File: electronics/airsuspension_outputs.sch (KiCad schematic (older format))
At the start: 51 parts, among them Q1 BSS138, Q2 BC847, U1 ITS5215L, U2 BTS6133D, U3 ITS5215L, U4 ITS5215L, U5 ITS5215L

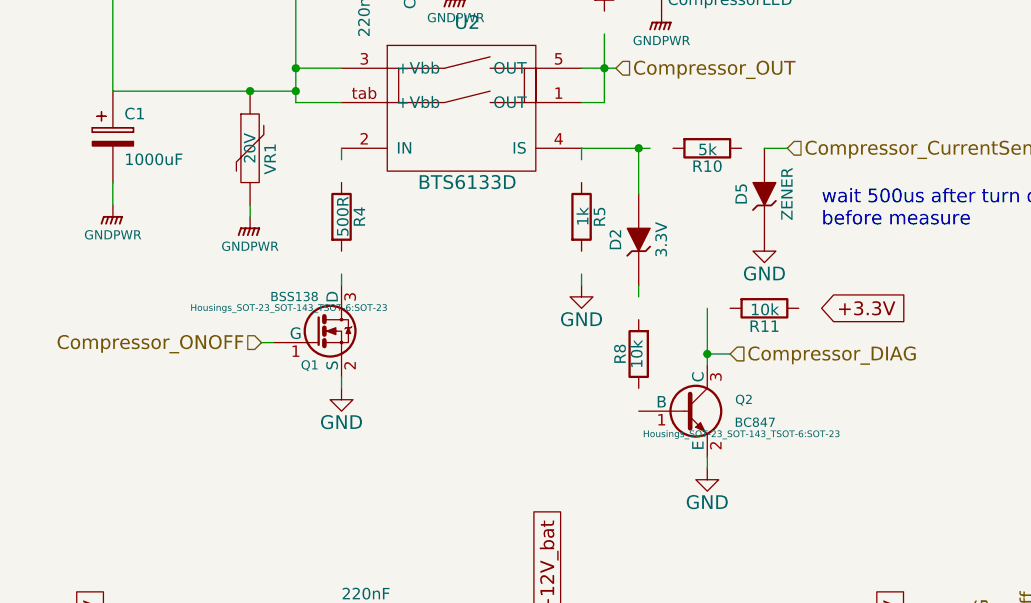
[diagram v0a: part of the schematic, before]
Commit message: Some more fottprints added to PCB
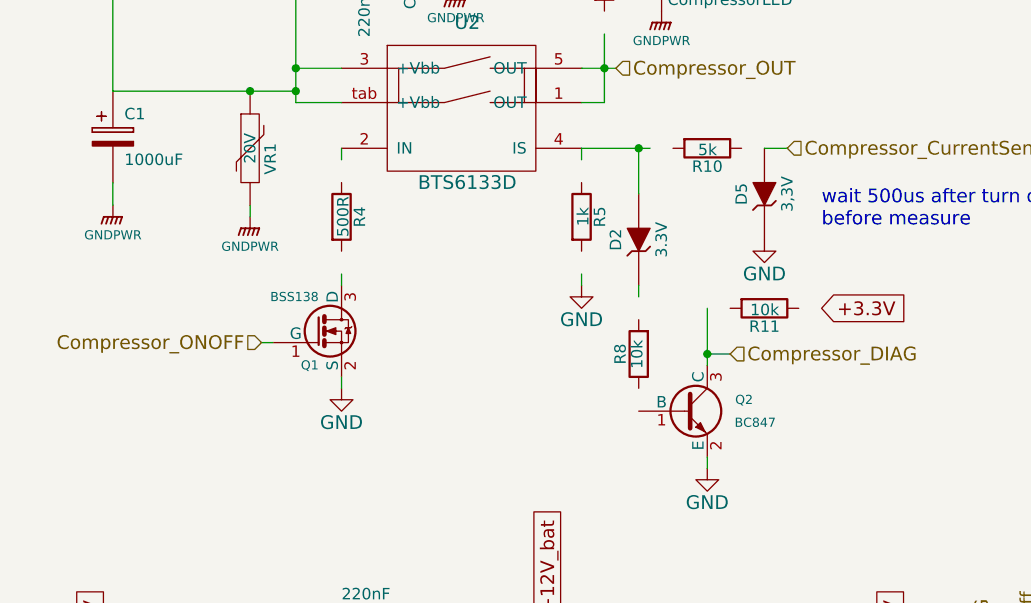
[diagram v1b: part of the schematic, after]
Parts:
- C2, C3, C4, C5, C6: footprint (none) -> Capacitors_SMD:C_0805; farnell (none) -> 1288261; name (none) -> C0805C224K5RACTU
- D2: footprint (none) -> Diodes_SMD:SOD-323
- D5: value ZENER -> 3,3V; footprint (none) -> Diodes_SMD:SOD-323
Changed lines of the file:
@@
 F 0 "C3" H 2750 1200 50  0000 L CNN
 F 1 "220nF" H 2750 1000 50  0000 L CNN
-F 2 "" H 2738 950 30  0001 C CNN
+F 2 "Capacitors_SMD:C_0805" H 2738 950 30  0001 C CNN
 F 3 "" H 2700 1100 60  0000 C CNN
+F 4 "1288261" H 2700 1100 60  0001 C CNN "farnell"
+F 5 "C0805C224K5RACTU" H 2700 1100 60  0001 C CNN "name"
 	1    2700 1100
 	0    1    1    0
@@
 F 0 "C2" H 2650 4050 50  0000 L CNN
 F 1 "220nF" V 2450 3850 50  0000 L CNN
-F 2 "" H 2638 3800 30  0001 C CNN
+F 2 "Capacitors_SMD:C_0805" H 2638 3800 30  0001 C CNN
 F 3 "" H 2600 3950 60  0000 C CNN
+F 4 "1288261" H 2600 3950 60  0001 C CNN "farnell"
+F 5 "C0805C224K5RACTU" H 2600 3950 60  0001 C CNN "name"
 	1    2600 3950
 	0    1    1    0
@@
 F 0 "D2" H 3800 2350 50  0000 C CNN
 F 1 "3.3V" H 3800 2150 50  0000 C CNN
-F 2 "" H 3800 2250 60  0001 C CNN
+F 2 "Diodes_SMD:SOD-323" H 3800 2250 60  0001 C CNN
 F 3 "" H 3800 2250 60  0000 C CNN
 F 4 "PDZ3.3B,115" H 3800 2250 60  0001 C CNN "name"
@@
 P 4350 2050
 F 0 "D5" H 4350 2150 50  0000 C CNN
-F 1 "ZENER" H 4350 1950 50  0000 C CNN
-F 2 "" H 4350 2050 60  0001 C CNN
+F 1 "3,3V" H 4350 1950 50  0000 C CNN
+F 2 "Diodes_SMD:SOD-323" H 4350 2050 60  0001 C CNN
 F 3 "" H 4350 2050 60  0000 C CNN
 F 4 "PDZ3.3B,115" H 4350 2050 60  0001 C CNN "name"
@@
 F 0 "C5" H 8300 1100 50  0000 L CNN
 F 1 "220nF" V 8100 900 50  0000 L CNN
-F 2 "" H 8288 850 30  0001 C CNN
+F 2 "Capacitors_SMD:C_0805" H 8288 850 30  0001 C CNN
 F 3 "" H 8250 1000 60  0000 C CNN
+F 4 "1288261" H 8250 1000 60  0001 C CNN "farnell"
+F 5 "C0805C224K5RACTU" H 8250 1000 60  0001 C CNN "name"
 	1    8250 1000
 	0    1    1    0
@@
 F 0 "C6" H 9350 4050 50  0000 L CNN
 F 1 "220nF" V 9150 3850 50  0000 L CNN
-F 2 "" H 9338 3800 30  0001 C CNN
+F 2 "Capacitors_SMD:C_0805" H 9338 3800 30  0001 C CNN
 F 3 "" H 9300 3950 60  0000 C CNN
+F 4 "1288261" H 9300 3950 60  0001 C CNN "farnell"
+F 5 "C0805C224K5RACTU" H 9300 3950 60  0001 C CNN "name"
 	1    9300 3950
 	0    1    1    0
@@
 F 0 "C4" H 6150 4050 50  0000 L CNN
 F 1 "220nF" V 5950 3850 50  0000 L CNN
-F 2 "" H 6138 3800 30  0001 C CNN
+F 2 "Capacitors_SMD:C_0805" H 6138 3800 30  0001 C CNN
 F 3 "" H 6100 3950 60  0000 C CNN
+F 4 "1288261" H 6100 3950 60  0001 C CNN "farnell"
+F 5 "C0805C224K5RACTU" H 6100 3950 60  0001 C CNN "name"
 	1    6100 3950
 	0    1    1    0
@@
 F 0 "Q2" H 4300 3050 40  0000 R CNN
 F 1 "BC847" H 4400 2950 40  0000 R CNN
-F 2 "Housings_SOT-23_SOT-143_TSOT-6:SOT-23" H 4250 2900 29  0000 C CNN
+F 2 "Housings_SOT-23_SOT-143_TSOT-6:SOT-23" H 4250 2900 29  0001 C CNN
 F 3 "" H 4000 3000 60  0000 C CNN
 F 4 "1773609" H 4000 3000 60  0001 C CNN "farnell"
@@
 F 0 "Q1" H 2400 2501 40  0000 R CNN
 F 1 "BSS138" H 2400 2800 40  0000 R CNN
-F 2 "Housings_SOT-23_SOT-143_TSOT-6:SOT-23" H 2270 2752 29  0000 C CNN
+F 2 "Housings_SOT-23_SOT-143_TSOT-6:SOT-23" H 2270 2752 29  0001 C CNN
 F 3 "" H 2400 2650 60  0000 C CNN
 F 4 "2053833" H 2400 2650 60  0001 C CNN "farnell"

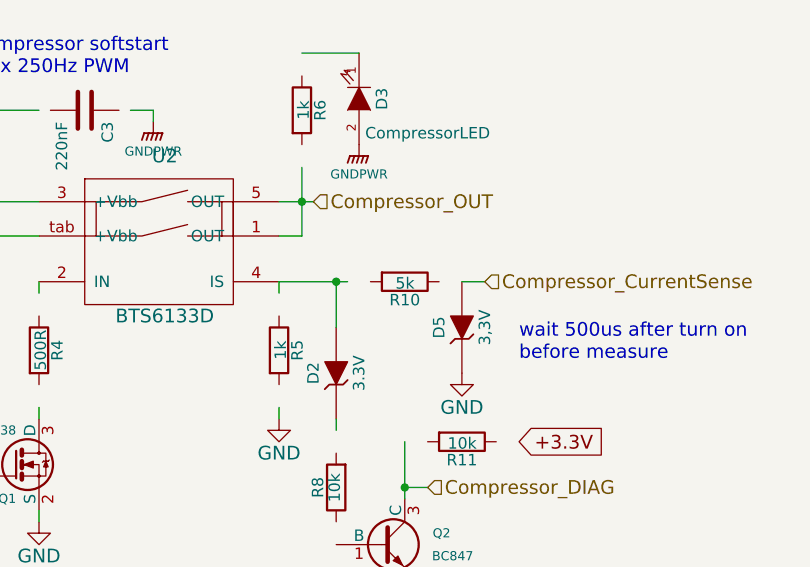
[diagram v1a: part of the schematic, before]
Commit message: some fottprints and BOM changes
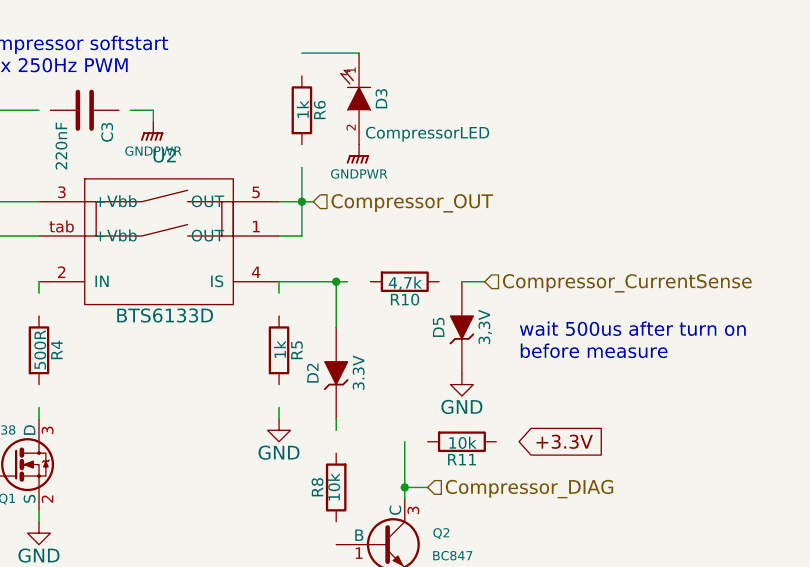
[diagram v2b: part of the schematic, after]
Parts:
- R1, R12, R13, R15, R16, R17, R18, R2, R20, R21, R23, R24, R25, R26, R5, R7, R9: footprint (none) -> Resistors_SMD:R_0805; farnell (none) -> 1577659; name (none) -> ERA6AEB102V
- R10: value 5k -> 4,7k; footprint (none) -> Resistors_SMD:R_0805; farnell (none) -> 2333572; name (none) -> CR0805-FX-4701ELF
- R11, R8: footprint (none) -> Resistors_SMD:R_0805; farnell (none) -> 612522; name (none) -> CR0805-FX-1002ELF
- R14, R19, R22, R3: footprint (none) -> Resistors_SMD:R_0805; farnell (none) -> 2303460; name (none) -> ERJ6ENF1500V
- R4: footprint (none) -> Resistors_SMD:R_0805; farnell (none) -> 2303491; name (none) -> ERJ6ENF3000V
- R6: footprint (none) -> Resistors_SMD:R_0805
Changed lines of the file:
@@
 F 0 "R4" V 2580 2150 50  0000 C CNN
 F 1 "500R" V 2507 2151 50  0000 C CNN
-F 2 "" V 2430 2150 30  0001 C CNN
+F 2 "Resistors_SMD:R_0805" V 2430 2150 30  0001 C CNN
 F 3 "" H 2500 2150 30  0000 C CNN
+F 4 "2303491" V 2500 2150 60  0001 C CNN "farnell"
+F 5 "ERJ6ENF3000V" V 2500 2150 60  0001 C CNN "name"
 	1    2500 2150
 	1    0    0    -1
@@
 F 0 "R5" V 3630 2150 50  0000 C CNN
 F 1 "1k" V 3557 2151 50  0000 C CNN
-F 2 "" V 3480 2150 30  0001 C CNN
+F 2 "Resistors_SMD:R_0805" V 3480 2150 30  0001 C CNN
 F 3 "" H 3550 2150 30  0000 C CNN
+F 4 "1577659" V 3550 2150 60  0001 C CNN "farnell"
+F 5 "ERA6AEB102V" V 3550 2150 60  0001 C CNN "name"
 	1    3550 2150
 	1    0    0    -1
@@
 F 0 "R8" V 3880 2750 50  0000 C CNN
 F 1 "10k" V 3807 2751 50  0000 C CNN
-F 2 "" V 3730 2750 30  0001 C CNN
+F 2 "Resistors_SMD:R_0805" V 3730 2750 30  0001 C CNN
 F 3 "" H 3800 2750 30  0000 C CNN
+F 4 "CR0805-FX-1002ELF" V 3800 2750 60  0001 C CNN "name"
+F 5 "612522" V 3800 2750 60  0001 C CNN "farnell"
 	1    3800 2750
 	-1   0    0    1
@@
 P 4100 1850
 F 0 "R10" V 4180 1850 50  0000 C CNN
-F 1 "5k" V 4107 1851 50  0000 C CNN
-F 2 "" V 4030 1850 30  0001 C CNN
+F 1 "4,7k" V 4107 1851 50  0000 C CNN
+F 2 "Resistors_SMD:R_0805" V 4030 1850 30  0001 C CNN
 F 3 "" H 4100 1850 30  0000 C CNN
+F 4 "2333572" V 4100 1850 60  0001 C CNN "farnell"
+F 5 "CR0805-FX-4701ELF" V 4100 1850 60  0001 C CNN "name"
 	1    4100 1850
 	0    1    1    0
@@
 F 0 "R11" V 4430 2550 50  0000 C CNN
 F 1 "10k" V 4357 2551 50  0000 C CNN
-F 2 "" V 4280 2550 30  0001 C CNN
+F 2 "Resistors_SMD:R_0805" V 4280 2550 30  0001 C CNN
 F 3 "" H 4350 2550 30  0000 C CNN
+F 4 "612522" V 4350 2550 60  0001 C CNN "farnell"
+F 5 "CR0805-FX-1002ELF" V 4350 2550 60  0001 C CNN "name"
 	1    4350 2550
 	0    1    1    0
@@
 F 0 "R6" V 3730 1100 50  0000 C CNN
 F 1 "1k" V 3657 1101 50  0000 C CNN
-F 2 "" V 3580 1100 30  0001 C CNN
+F 2 "Resistors_SMD:R_0805" V 3580 1100 30  0001 C CNN
 F 3 "" H 3650 1100 30  0000 C CNN
 	1    3650 1100
@@
 F 0 "R2" V 1680 4500 50  0000 C CNN
 F 1 "1k" V 1607 4501 50  0000 C CNN
-F 2 "" V 1530 4500 30  0001 C CNN
+F 2 "Resistors_SMD:R_0805" V 1530 4500 30  0001 C CNN
 F 3 "" H 1600 4500 30  0000 C CNN
+F 4 "ERA6AEB102V" V 1600 4500 60  0001 C CNN "name"
+F 5 "1577659" V 1600 4500 60  0001 C CNN "farnell"
 	1    1600 4500
 	-1   0    0    1
@@
 F 0 "R1" V 1480 4500 50  0000 C CNN
 F 1 "1k" V 1407 4501 48  0000 C CNN
-F 2 "" V 1330 4500 30  0001 C CNN
+F 2 "Resistors_SMD:R_0805" V 1330 4500 30  0001 C CNN
 F 3 "" H 1400 4500 30  0000 C CNN
+F 4 "ERA6AEB102V" V 1400 4500 60  0001 C CNN "name"
+F 5 "1577659" V 1400 4500 60  0001 C CNN "farnell"
 	1    1400 4500
 	-1   0    0    1
@@
 F 0 "R7" V 3730 5400 50  0000 C CNN
 F 1 "1k" V 3657 5401 50  0000 C CNN
-F 2 "" V 3580 5400 30  0001 C CNN
+F 2 "Resistors_SMD:R_0805" V 3580 5400 30  0001 C CNN
 F 3 "" H 3650 5400 30  0000 C CNN
+F 4 "ERA6AEB102V" V 3650 5400 60  0001 C CNN "name"
+F 5 "1577659" V 3650 5400 60  0001 C CNN "farnell"
 	1    3650 5400
 	-1   0    0    1
@@
 F 0 "R9" V 3980 5400 50  0000 C CNN
 F 1 "1k" V 3907 5401 50  0000 C CNN
-F 2 "" V 3830 5400 30  0001 C CNN
+F 2 "Resistors_SMD:R_0805" V 3830 5400 30  0001 C CNN
 F 3 "" H 3900 5400 30  0000 C CNN
+F 4 "ERA6AEB102V" V 3900 5400 60  0001 C CNN "name"
+F 5 "1577659" V 3900 5400 60  0001 C CNN "farnell"
 	1    3900 5400
 	1    0    0    -1
@@
 F 0 "R3" V 2230 4200 50  0000 C CNN
 F 1 "150R" V 2157 4201 50  0000 C CNN
-F 2 "" V 2080 4200 30  0001 C CNN
+F 2 "Resistors_SMD:R_0805" V 2080 4200 30  0001 C CNN
 F 3 "" H 2150 4200 30  0000 C CNN
+F 4 "ERJ6ENF1500V" V 2150 4200 60  0001 C CNN "name"
+F 5 "2303460" V 2150 4200 60  0001 C CNN "farnell"
 	1    2150 4200
 	1    0    0    -1
@@
 F 0 "R17" V 7330 1550 50  0000 C CNN
 F 1 "1k" V 7257 1551 50  0000 C CNN
-F 2 "" V 7180 1550 30  0001 C CNN
+F 2 "Resistors_SMD:R_0805" V 7180 1550 30  0001 C CNN
 F 3 "" H 7250 1550 30  0000 C CNN
+F 4 "ERA6AEB102V" V 7250 1550 60  0001 C CNN "name"
+F 5 "1577659" V 7250 1550 60  0001 C CNN "farnell"
 	1    7250 1550
 	-1   0    0    1
@@
 F 0 "R15" V 7130 1550 50  0000 C CNN
 F 1 "1k" V 7057 1551 48  0000 C CNN
-F 2 "" V 6980 1550 30  0001 C CNN
+F 2 "Resistors_SMD:R_0805" V 6980 1550 30  0001 C CNN
 F 3 "" H 7050 1550 30  0000 C CNN
+F 4 "ERA6AEB102V" V 7050 1550 60  0001 C CNN "name"
+F 5 "1577659" V 7050 1550 60  0001 C CNN "farnell"
 	1    7050 1550
 	-1   0    0    1
@@
 F 0 "R23" V 9380 2450 50  0000 C CNN
 F 1 "1k" V 9307 2451 50  0000 C CNN
-F 2 "" V 9230 2450 30  0001 C CNN
+F 2 "Resistors_SMD:R_0805" V 9230 2450 30  0001 C CNN
 F 3 "" H 9300 2450 30  0000 C CNN
+F 4 "ERA6AEB102V" V 9300 2450 60  0001 C CNN "name"
+F 5 "1577659" V 9300 2450 60  0001 C CNN "farnell"
 	1    9300 2450
 	-1   0    0    1
@@
 F 0 "R24" V 9630 2450 50  0000 C CNN
 F 1 "1k" V 9557 2451 50  0000 C CNN
-F 2 "" V 9480 2450 30  0001 C CNN
+F 2 "Resistors_SMD:R_0805" V 9480 2450 30  0001 C CNN
 F 3 "" H 9550 2450 30  0000 C CNN
+F 4 "ERA6AEB102V" V 9550 2450 60  0001 C CNN "name"
+F 5 "1577659" V 9550 2450 60  0001 C CNN "farnell"
 	1    9550 2450
 	1    0    0    -1
@@
 F 0 "R19" V 7880 1250 50  0000 C CNN
 F 1 "150R" V 7807 1251 50  0000 C CNN
-F 2 "" V 7730 1250 30  0001 C CNN
+F 2 "Resistors_SMD:R_0805" V 7730 1250 30  0001 C CNN
 F 3 "" H 7800 1250 30  0000 C CNN
+F 4 "2303460" V 7800 1250 60  0001 C CNN "farnell"
+F 5 "ERJ6ENF1500V" V 7800 1250 60  0001 C CNN "name"
 	1    7800 1250
 	1    0    0    -1
@@
 F 0 "R21" V 8380 4500 50  0000 C CNN
 F 1 "1k" V 8307 4501 50  0000 C CNN
-F 2 "" V 8230 4500 30  0001 C CNN
+F 2 "Resistors_SMD:R_0805" V 8230 4500 30  0001 C CNN
 F 3 "" H 8300 4500 30  0000 C CNN
+F 4 "ERA6AEB102V" V 8300 4500 60  0001 C CNN "name"
+F 5 "1577659" V 8300 4500 60  0001 C CNN "farnell"
 	1    8300 4500
 	-1   0    0    1
@@
 F 0 "R20" V 8180 4500 50  0000 C CNN
 F 1 "1k" V 8107 4501 48  0000 C CNN
-F 2 "" V 8030 4500 30  0001 C CNN
+F 2 "Resistors_SMD:R_0805" V 8030 4500 30  0001 C CNN
 F 3 "" H 8100 4500 30  0000 C CNN
+F 4 "ERA6AEB102V" V 8100 4500 60  0001 C CNN "name"
+F 5 "1577659" V 8100 4500 60  0001 C CNN "farnell"
 	1    8100 4500
 	-1   0    0    1
@@
 F 0 "R25" V 10430 5400 50  0000 C CNN
 F 1 "1k" V 10357 5401 50  0000 C CNN
-F 2 "" V 10280 5400 30  0001 C CNN
+F 2 "Resistors_SMD:R_0805" V 10280 5400 30  0001 C CNN
 F 3 "" H 10350 5400 30  0000 C CNN
+F 4 "ERA6AEB102V" V 10350 5400 60  0001 C CNN "name"
+F 5 "1577659" V 10350 5400 60  0001 C CNN "farnell"
 	1    10350 5400
 	-1   0    0    1
@@
 F 0 "R26" V 10680 5400 50  0000 C CNN
 F 1 "1k" V 10607 5401 50  0000 C CNN
-F 2 "" V 10530 5400 30  0001 C CNN
+F 2 "Resistors_SMD:R_0805" V 10530 5400 30  0001 C CNN
 F 3 "" H 10600 5400 30  0000 C CNN
+F 4 "ERA6AEB102V" V 10600 5400 60  0001 C CNN "name"
+F 5 "1577659" V 10600 5400 60  0001 C CNN "farnell"
 	1    10600 5400
 	1    0    0    -1
@@
 F 0 "R22" V 8930 4200 50  0000 C CNN
 F 1 "150R" V 8857 4201 50  0000 C CNN
-F 2 "" V 8780 4200 30  0001 C CNN
+F 2 "Resistors_SMD:R_0805" V 8780 4200 30  0001 C CNN
 F 3 "" H 8850 4200 30  0000 C CNN
+F 4 "ERJ6ENF1500V" V 8850 4200 60  0001 C CNN "name"
+F 5 "2303460" V 8850 4200 60  0001 C CNN "farnell"
 	1    8850 4200
 	1    0    0    -1
@@
 F 0 "R13" V 5180 4500 50  0000 C CNN
 F 1 "1k" V 5107 4501 50  0000 C CNN
-F 2 "" V 5030 4500 30  0001 C CNN
+F 2 "Resistors_SMD:R_0805" V 5030 4500 30  0001 C CNN
 F 3 "" H 5100 4500 30  0000 C CNN
+F 4 "ERA6AEB102V" V 5100 4500 60  0001 C CNN "name"
+F 5 "1577659" V 5100 4500 60  0001 C CNN "farnell"
 	1    5100 4500
 	-1   0    0    1
@@
 F 0 "R12" V 4980 4500 50  0000 C CNN
 F 1 "1k" V 4907 4501 48  0000 C CNN
-F 2 "" V 4830 4500 30  0001 C CNN
+F 2 "Resistors_SMD:R_0805" V 4830 4500 30  0001 C CNN
 F 3 "" H 4900 4500 30  0000 C CNN
+F 4 "ERA6AEB102V" V 4900 4500 60  0001 C CNN "name"
+F 5 "1577659" V 4900 4500 60  0001 C CNN "farnell"
 	1    4900 4500
 	-1   0    0    1
@@
 F 0 "R16" V 7230 5400 50  0000 C CNN
 F 1 "1k" V 7157 5401 50  0000 C CNN
-F 2 "" V 7080 5400 30  0001 C CNN
+F 2 "Resistors_SMD:R_0805" V 7080 5400 30  0001 C CNN
 F 3 "" H 7150 5400 30  0000 C CNN
+F 4 "ERA6AEB102V" V 7150 5400 60  0001 C CNN "name"
+F 5 "1577659" V 7150 5400 60  0001 C CNN "farnell"
 	1    7150 5400
 	-1   0    0    1
@@
 F 0 "R18" V 7480 5400 50  0000 C CNN
 F 1 "1k" V 7407 5401 50  0000 C CNN
-F 2 "" V 7330 5400 30  0001 C CNN
+F 2 "Resistors_SMD:R_0805" V 7330 5400 30  0001 C CNN
 F 3 "" H 7400 5400 30  0000 C CNN
+F 4 "ERA6AEB102V" V 7400 5400 60  0001 C CNN "name"
+F 5 "1577659" V 7400 5400 60  0001 C CNN "farnell"
 	1    7400 5400
 	1    0    0    -1
@@
 F 0 "R14" V 5730 4200 50  0000 C CNN
 F 1 "150R" V 5657 4201 50  0000 C CNN
-F 2 "" V 5580 4200 30  0001 C CNN
+F 2 "Resistors_SMD:R_0805" V 5580 4200 30  0001 C CNN
 F 3 "" H 5650 4200 30  0000 C CNN
+F 4 "ERJ6ENF1500V" V 5650 4200 60  0001 C CNN "name"
+F 5 "2303460" V 5650 4200 60  0001 C CNN "farnell"
 	1    5650 4200
 	1    0    0    -1

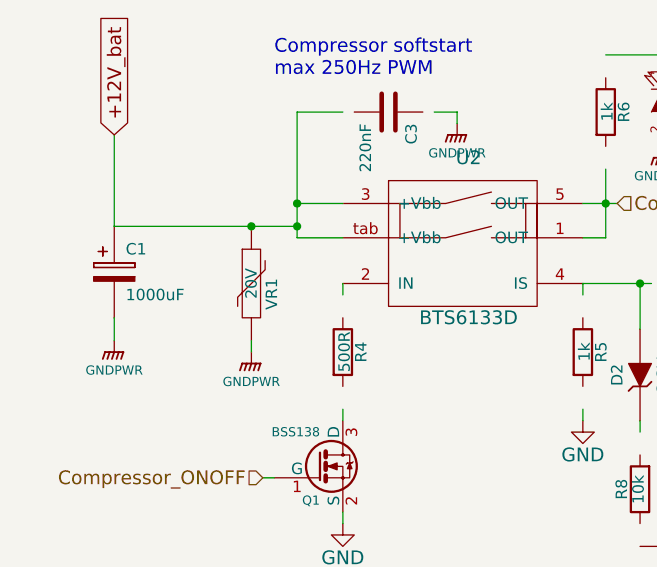
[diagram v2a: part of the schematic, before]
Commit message: Some more footprints and beginning PCB work
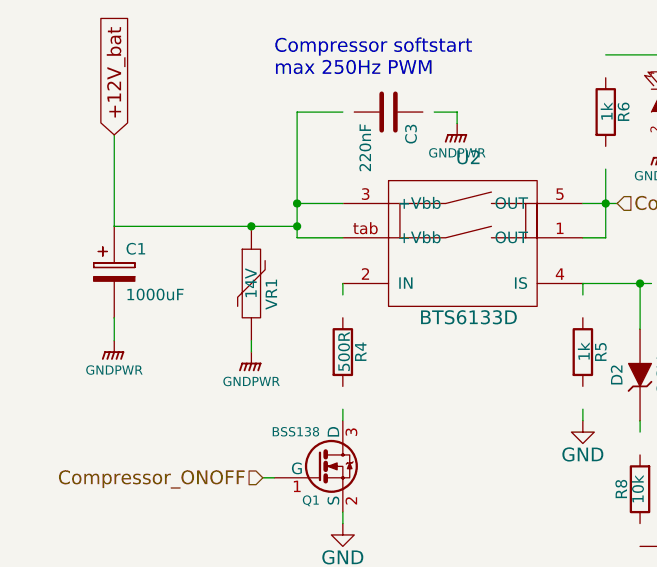
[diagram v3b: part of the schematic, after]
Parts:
- C1: footprint (none) -> kicad_lib:SMD_Cap_16x16.5
- U1, U3, U4, U5: footprint (none) -> kicad_lib:PG-DSO-12-2
- VR1: value 20V -> 14V; footprint (none) -> Resistors_SMD:R_1206_HandSoldering; farnell 1057155 -> 1863849; name V8ZA2P -> V14MLA1206NHAUTO
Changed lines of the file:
@@
 F 0 "U1" H 2450 5400 60  0000 C CNN
 F 1 "ITS5215L" H 2950 5400 60  0000 C CNN
-F 2 "" H 2750 4950 60  0001 C CNN
+F 2 "kicad_lib:PG-DSO-12-2" H 2750 4950 60  0001 C CNN
 F 3 "http://www.farnell.com/datasheets/85674.pdf" H 2750 4950 60  0001 C CNN
 F 4 "ITS5215L" H 2750 4850 60  0001 C CNN "name"
@@
 P 2100 1850
 F 0 "VR1" V 2160 1804 50  0000 C TNN
-F 1 "20V" V 2100 1850 50  0000 C CNN
-F 2 "" H 2100 1850 60  0001 C CNN
-F 3 "http://www.littelfuse.com/data/en/Data_Sheets/ZA.pdf" H 2100 1850 60  0001 C CNN
-F 4 "V8ZA2P" V 2100 1850 60  0001 C CNN "name"
-F 5 "1057155" V 2100 1850 60  0001 C CNN "farnell"
+F 1 "14V" V 2100 1850 50  0000 C CNN
+F 2 "Resistors_SMD:R_1206_HandSoldering" H 2100 1850 60  0001 C CNN
+F 3 "http://www.farnell.com/datasheets/1228202.pdf" H 2100 1850 60  0001 C CNN
+F 4 "V14MLA1206NHAUTO" V 2100 1850 60  0001 C CNN "name"
+F 5 "1863849" V 2100 1850 60  0001 C CNN "farnell"
 	1    2100 1850
 	1    0    0    -1
@@
 F 0 "C1" H 1550 1900 50  0000 L CNN
 F 1 "1000uF" H 1550 1700 50  0000 L CNN
-F 2 "" H 1538 1650 30  0001 C CNN
+F 2 "kicad_lib:SMD_Cap_16x16.5" H 1538 1650 30  0001 C CNN
 F 3 "http://www.farnell.com/datasheets/1884702.pdf" H 1500 1800 60  0001 C CNN
 F 4 "EEEFK1H102AM" H 1500 1800 60  0001 C CNN "name"
@@
 F 0 "U4" H 8100 2450 60  0000 C CNN
 F 1 "ITS5215L" H 8600 2450 60  0000 C CNN
-F 2 "" H 8400 2000 60  0001 C CNN
+F 2 "kicad_lib:PG-DSO-12-2" H 8400 2000 60  0001 C CNN
 F 3 "" H 8400 2000 60  0000 C CNN
 F 4 "1426197" H 8400 1900 60  0001 C CNN "farnell"
@@
 F 0 "U5" H 9150 5400 60  0000 C CNN
 F 1 "ITS5215L" H 9650 5400 60  0000 C CNN
-F 2 "" H 9450 4950 60  0001 C CNN
+F 2 "kicad_lib:PG-DSO-12-2" H 9450 4950 60  0001 C CNN
 F 3 "" H 9450 4950 60  0000 C CNN
 F 4 "1426197" H 9450 4850 60  0001 C CNN "farnell"
@@
 F 0 "U3" H 5950 5400 60  0000 C CNN
 F 1 "ITS5215L" H 6450 5400 60  0000 C CNN
-F 2 "" H 6250 4950 60  0001 C CNN
+F 2 "kicad_lib:PG-DSO-12-2" H 6250 4950 60  0001 C CNN
 F 3 "" H 6250 4950 60  0000 C CNN
 F 4 "1426197" H 6250 4850 60  0001 C CNN "farnell"
